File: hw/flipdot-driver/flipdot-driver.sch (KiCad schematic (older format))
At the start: 98 parts, among them J1 DISPLAY, J2 NRF_CON, J3 Prog, J4 I2C, J5 USART, J6 USB, J7 USB_B_Micro, J8 RST, J9 MAIN_Power, Q1 MMBTA64, Q10 MMBTA64, Q11 MMBTA64, Q12 MMBTA64, Q13 MMBTA64, Q14 MMBTA64, Q15 Q_NMOS_GSD, Q16 Q_NMOS_GSD, Q17 Q_NMOS_GSD, Q18 Q_NMOS_GSD, Q2 MMBTA64, Q3 MMBTA64, Q4 MMBTA64, Q5 MMBTA64, Q6 MMBTA64, Q7 MMBTA64, Q8 MMBTA64, Q9 MMBTA64, U1 AT25xxx, U2 ULN2003A, U3 USBLC6-2SC6, U4 AZ1117-3.3, U5 ULN2003A, U6 stm32_STM32F103C(8-B)Tx, U7 74HC595, U8 AX5201, U9 74HC595, Y1 32768, Y2 8MHz/20pF

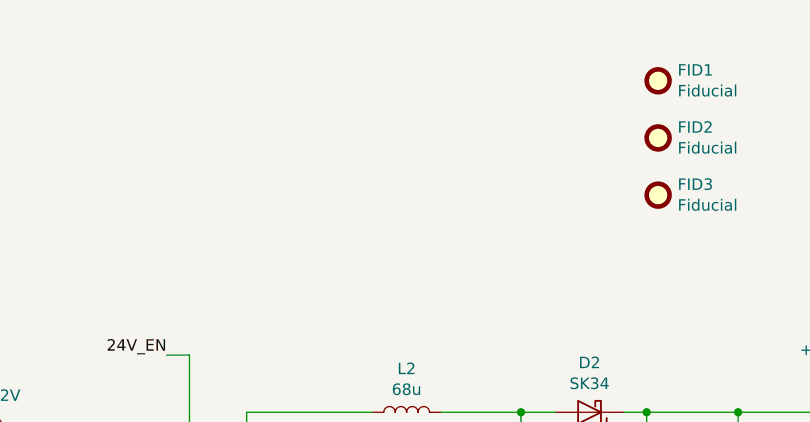
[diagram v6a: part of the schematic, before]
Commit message: Better ground planes.
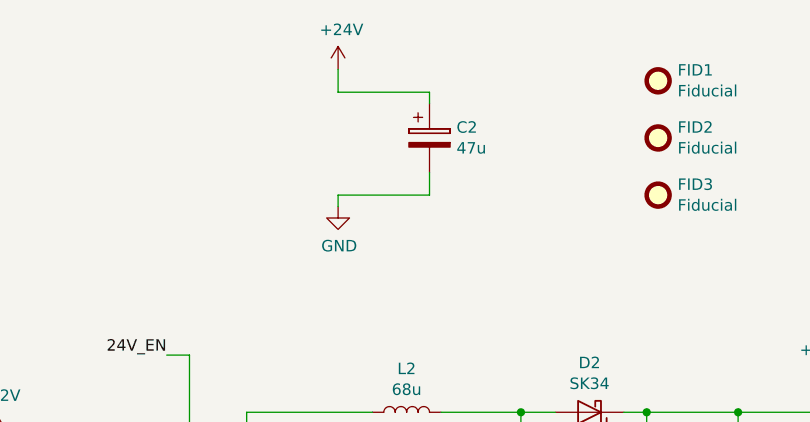
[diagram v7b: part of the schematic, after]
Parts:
- added C2: 47u, Capacitor_THT:CP_Radial_D6.3mm_P2.50mm, symbol flipdot-driver-rescue:CP-controller-cache-flipdot-driver-rescue-flipdot-driver-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
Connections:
- net +24V: now also C2.1
- net GND: now also C2.2
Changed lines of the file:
@@
 	1    0    0    -1
 $EndComp
+$Comp
+L power:+24V #PWR01
+U 1 1 5CF7E71E
+P 2300 850
+F 0 "#PWR01" H 2300 700 50  0001 C CNN
+F 1 "+24V" H 2315 1023 50  0000 C CNN
+F 2 "" H 2300 850 50  0001 C CNN
+F 3 "" H 2300 850 50  0001 C CNN
+	1    2300 850
+	1    0    0    -1
+$EndComp
+$Comp
+L power:GND #PWR02
+U 1 1 5CF803D6
+P 2300 1450
+F 0 "#PWR02" H 2300 1200 50  0001 C CNN
+F 1 "GND" H 2305 1277 50  0000 C CNN
+F 2 "" H 2300 1450 50  0001 C CNN
+F 3 "" H 2300 1450 50  0001 C CNN
+	1    2300 1450
+	1    0    0    -1
+$EndComp
+$Comp
+L flipdot-driver-rescue:CP-controller-cache-flipdot-driver-rescue-flipdot-driver-rescue-flipdot-driver-rescue C2
+U 1 1 5CF80FCA
+P 2700 1150
+F 0 "C2" H 2818 1196 50  0000 L CNN
+F 1 "47u" H 2818 1105 50  0000 L CNN
+F 2 "Capacitor_THT:CP_Radial_D6.3mm_P2.50mm" H 2738 1000 50  0001 C CNN
+F 3 "" H 2700 1150 50  0001 C CNN
+	1    2700 1150
+	1    0    0    -1
+$EndComp
+Wire Wire Line
+	2300 1400 2700 1400
+Wire Wire Line
+	2700 1400 2700 1300
+Wire Wire Line
+	2300 1400 2300 1450
+Wire Wire Line
+	2300 850  2300 950
+Wire Wire Line
+	2300 950  2700 950
+Wire Wire Line
+	2700 950  2700 1000
 $EndSCHEMATC
